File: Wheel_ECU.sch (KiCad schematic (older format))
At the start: 20 parts, among them J1 Conn_01x04, J2 Conn_01x04, J3 Conn_01x02, J4 Debug, U1 BD6211F, U2 TLE4964, U3 XMC1404_F064, U4 TLE7251

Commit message: Replace the motor driver and other improvements
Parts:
- removed R1, R2: 10K, Resistors_SMD:R_0805_HandSoldering, symbol R
- removed U1: BD6211F, Housings_SOIC:SO-8_5.3x6.2mm_Pitch1.27mm, symbol BD6211F
- added C10: 100uF, Capacitors_SMD:C_0805_HandSoldering, symbol Wheel_ECU-rescue:C
- added U1: IFX9201SG, WheelECU:SOIC-12_HeatSlugs, symbol wheel_ecu:IFX9201SG
- C1: value 10uF -> 1uF; symbol C -> Wheel_ECU-rescue:C
- C2, C3, C4, C5, C6, C7, C8, C9: symbol C -> Wheel_ECU-rescue:C
- D1: value TVS_Diode -> SMF5.0A; footprint Diodes_SMD:D_SOD-323_HandSoldering -> Diodes_SMD:D_MELF; symbol TVS_Diode -> Wheel_ECU-rescue:TVS_Diode
- J1, J2: symbol Conn_01x04 -> Wheel_ECU-rescue:Conn_01x04
- J3: symbol Conn_01x02 -> Wheel_ECU-rescue:Conn_01x02
- J4: footprint Pin_Headers:Pin_Header_Straight_2x04_Pitch2.54mm_SMD -> WheelECU:Pin_Header_Straight_2x04_Pitch2.54mm_SMD; symbol Conn_02x04_Odd_Even -> Wheel_ECU-rescue:Conn_02x04_Odd_Even
- U2: symbol TLE4964 -> Wheel_ECU-rescue:TLE4964
- U3: footprint Housings_QFP:TQFP-64_10x10mm_Pitch0.5mm -> WheelECU:TQFP-64_10x10mm_Pitch0.5mm_Handsoldering; symbol XMC1404_F064 -> Wheel_ECU-rescue:XMC1404_F064
- U4: symbol TLE7251 -> Wheel_ECU-rescue:TLE7251
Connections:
- net +5V: now also C1.2, D1.1, C10.2, U1.2 (VSO), U1.4 (VS); no longer C1.1, D1.2
- net GND: now also C1.1, D1.2, C10.1, U1.6 (GND); no longer C1.2, D1.1
- net MOSI: now reaches U3.10 (P2.1)
- net MOSI: now also U1.8 (SI)
- net MISO: now reaches U3.11 (P2.2)
- net MISO: now also U1.3 (SO)
- net MOTOR_DRIVER_SS: now reaches U3.28 (P1.6)
- net MOTOR_DRIVER_SS: now also U1.9 (CSN)
- net MOTOR_DISABLE: now reaches U3.62 (P4.3)
- net MOTOR_DISABLE: now also U1.11 (DIS)
- net SCLK: now reaches U3.9 (P2.0)
- net SCLK: now also U1.10 (SCK)
- net MOTOR_OUT1: now reaches J3.1 (Pin_1)
- net MOTOR_OUT1: now also U1.5 (OUT1)
- net MOTOR_OUT2: now reaches J3.2 (Pin_2)
- net MOTOR_OUT2: now also U1.7 (OUT2)
- net MOTOR_FORWARD renamed MOTOR_PWM
- net MOTOR_PWM: now also U1.12 (PWM)
- net MOTOR_REVERSE renamed MOTOR_DIRECTION
- net MOTOR_DIRECTION: now also U1.1 (DIR)
- no-connect marks 46 -> 41
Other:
- moved on the sheet: C1, C2, C3, C4, C5, C6, C7, C8, C9, D1, J1, J2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

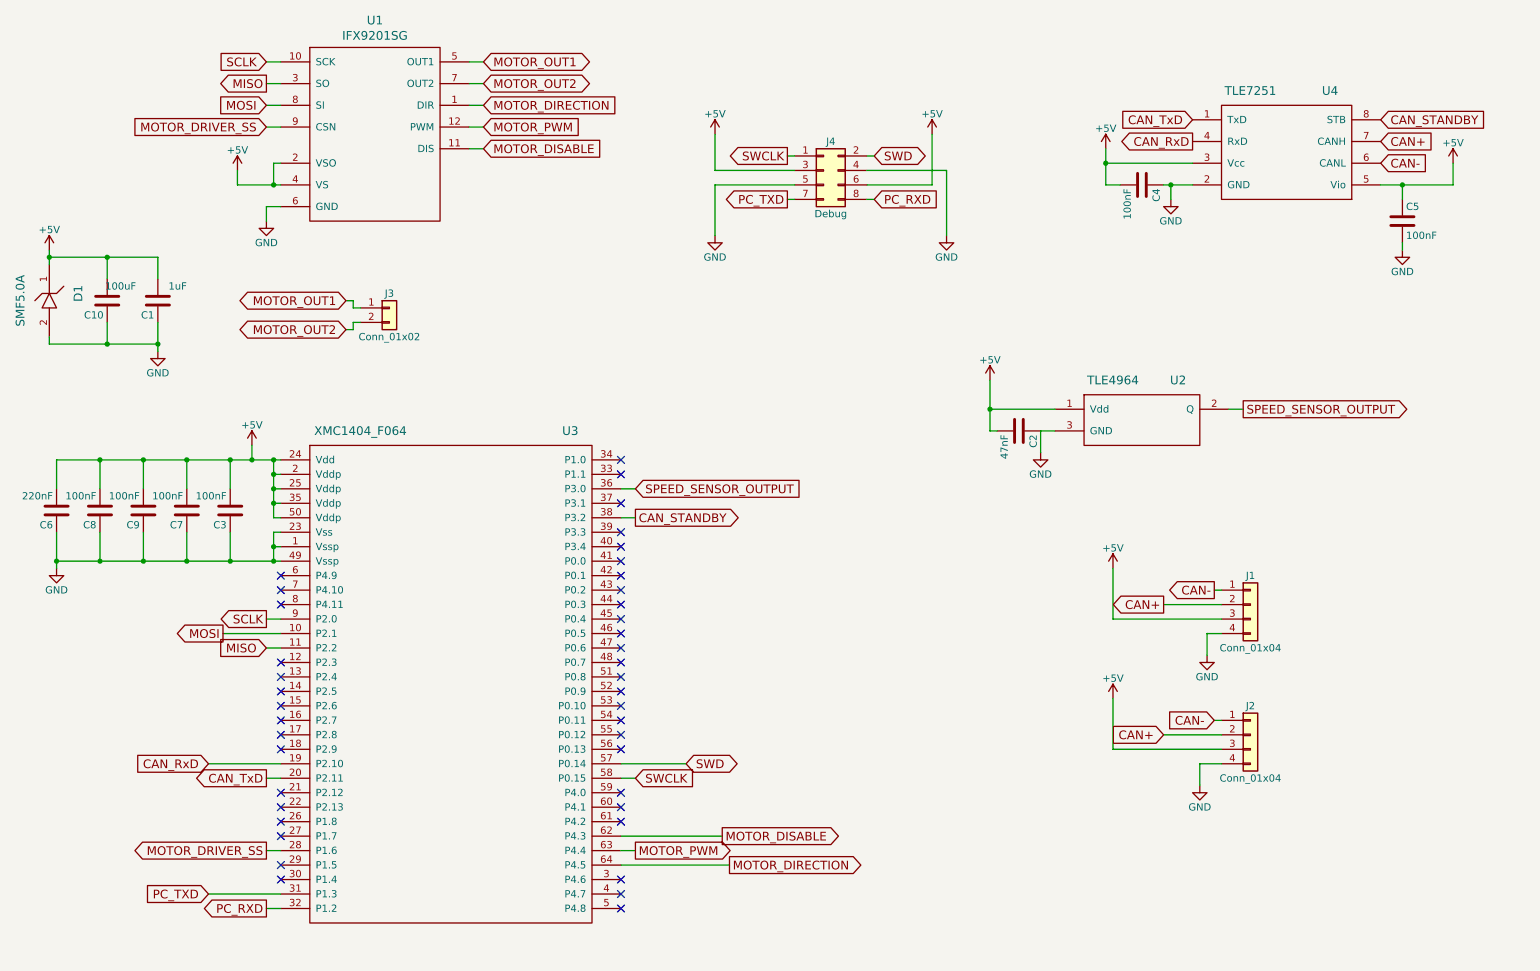
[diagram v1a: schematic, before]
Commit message: Copy the changes from the CentrifugalFan module
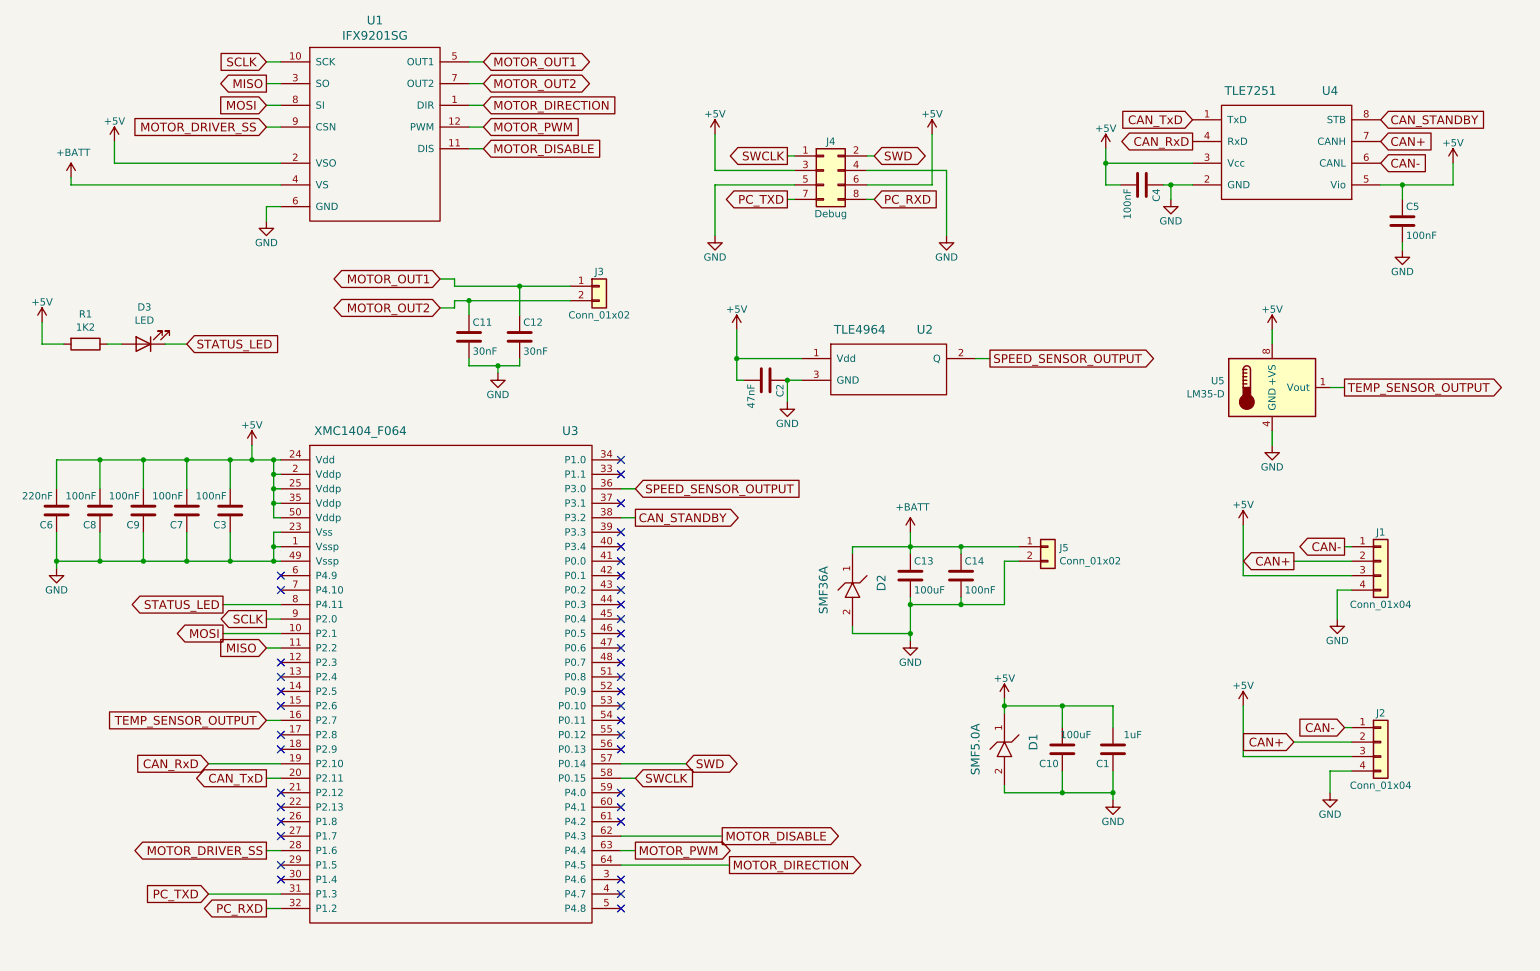
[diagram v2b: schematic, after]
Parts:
- added C11, C12: 30nF, WheelECU:C_0805_HandSoldering, symbol Wheel_ECU-rescue:C
- added C13: 100uF, WheelECU:C_0805_HandSoldering, symbol Wheel_ECU-rescue:C
- added C14: 100nF, WheelECU:C_0805_HandSoldering, symbol Wheel_ECU-rescue:C
- added D2: SMF36A, Diode_SMD:D_SOD-123F, symbol Wheel_ECU-rescue:TVS_Diode
- added D3: LED, WheelECU:C_0805_HandSoldering, symbol Device:LED
- added J5: Conn_01x02, Connector_PinHeader_2.54mm:PinHeader_1x02_P2.54mm_Vertical, symbol Connector_Generic:Conn_01x02
- added R1: 1K2, WheelECU:C_0805_HandSoldering, symbol Device:R
- added U5: LM35-D, Package_SO:SOIC-8_3.9x4.9mm_P1.27mm, symbol Sensor_Temperature:LM35-D
- D1: footprint Diodes_SMD:D_MELF -> Diode_SMD:D_SOD-123F
- J3: footprint Pin_Headers:Pin_Header_Straight_2x01_Pitch2.54mm_SMD -> Connector_PinHeader_2.54mm:PinHeader_1x02_P2.54mm_Vertical
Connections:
- net +5V: now also R1.2, U5.8 (+VS); no longer U1.4 (VS)
- net GND: now also C11.2, C12.2, C13.2, C14.2, D2.2, J5.2 (Pin_2), U5.4 (GND)
- net MOTOR_OUT1: now also C12.1
- net MOTOR_OUT2: now also C11.1
- net TEMP_SENSOR_OUTPUT: now reaches U3.16 (P2.7)
- net TEMP_SENSOR_OUTPUT: now also U5.1 (Vout)
- net STATUS_LED: now reaches U3.8 (P4.11)
- net STATUS_LED: now also D3.1 (K)
- new net: D3.2 (A), R1.1
- new net +BATT: C13.1, C14.1, D2.1, J5.1 (Pin_1), U1.4 (VS)
- no-connect marks 41 -> 39
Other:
- moved on the sheet: C1, C10, C2, D1, J1, J2, J3, U2
